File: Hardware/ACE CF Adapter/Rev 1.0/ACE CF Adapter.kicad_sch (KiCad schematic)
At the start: 8 parts, among them J21 STORAGE, J3 Compact Flash

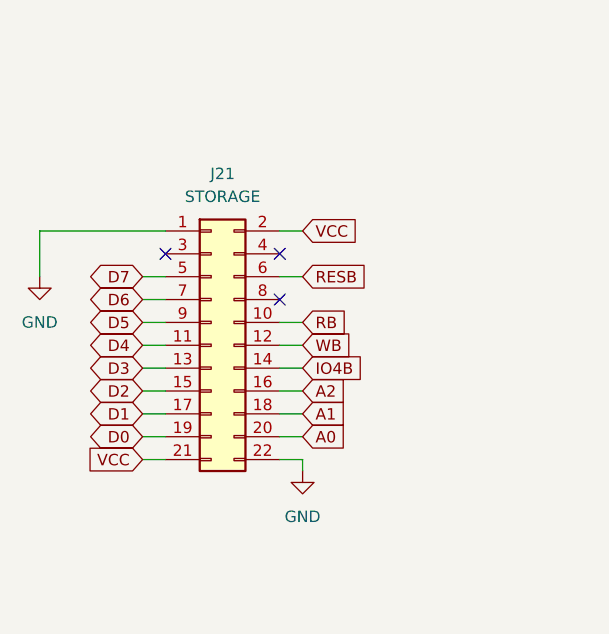
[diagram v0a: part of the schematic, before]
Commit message: Change storage header
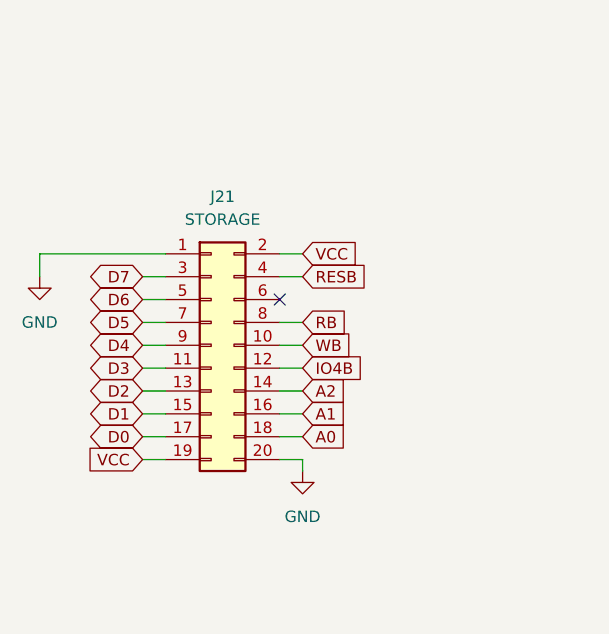
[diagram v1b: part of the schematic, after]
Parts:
- J21: footprint Connector_PinSocket_2.54mm:PinSocket_2x11_P2.54mm_Horizontal -> Connector_PinHeader_2.54mm:PinHeader_2x10_P2.54mm_Horizontal; symbol Connector_Generic:Conn_02x11_Odd_Even -> Connector_Generic:Conn_02x10_Odd_Even; Digikey S5557-ND S5560-ND S5564-ND -> (none); MPN PPPC042LJBN-RC PPPC072LJBN-RC PPPC112LJBN-RC -> (none)
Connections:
- net A0: now also J21.18 (Pin_18); no longer J21.20 (Pin_20)
- net A1: now also J21.16 (Pin_16); no longer J21.18 (Pin_18)
- net A2: now also J21.14 (Pin_14); no longer J21.16 (Pin_16)
- net D0: now also J21.17 (Pin_17); no longer J21.19 (Pin_19)
- net D1: now also J21.15 (Pin_15); no longer J21.17 (Pin_17)
- net D2: now also J21.13 (Pin_13); no longer J21.15 (Pin_15)
- net D3: now also J21.11 (Pin_11); no longer J21.13 (Pin_13)
- net D4: now also J21.9 (Pin_9); no longer J21.11 (Pin_11)
- net D5: now also J21.7 (Pin_7); no longer J21.9 (Pin_9)
- net D6: now also J21.5 (Pin_5); no longer J21.7 (Pin_7)
- net D7: now also J21.3 (Pin_3); no longer J21.5 (Pin_5)
- net GND: now also J21.20 (Pin_20); no longer J21.22 (Pin_22)
- net IO4B: now also J21.12 (Pin_12); no longer J21.14 (Pin_14)
- net RB: now also J21.8 (Pin_8); no longer J21.10 (Pin_10)
- net RESB: now also J21.4 (Pin_4); no longer J21.6 (Pin_6)
- net VCC: now also J21.19 (Pin_19); no longer J21.21 (Pin_21)
- net WB: now also J21.10 (Pin_10); no longer J21.12 (Pin_12)
- no-connect marks 18 -> 16
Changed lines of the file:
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@@
-	)
-	(no_connect
-		(at 58.42 78.74)
 	)
 	(no_connect
@@
 	)
 	(no_connect
-		(at 71.12 78.74)
-	)
-	(no_connect
 		(at 209.55 104.14)
 	)
@@
 	(wire
 		(pts
-			(xy 44.45 76.2) (xy 58.42 76.2)
-		)
-		(stroke
-			(width 0)
-			(type default)
-		)
-	)
-	(wire
-		(pts
-			(xy 44.45 76.2) (xy 44.45 81.28)
+			(xy 44.45 78.74) (xy 58.42 78.74)
+		)
+		(stroke
+			(width 0)
+			(type default)
+		)
+	)
+	(wire
+		(pts
+			(xy 44.45 78.74) (xy 44.45 81.28)
 		)
 		(stroke
@@
 	(wire
 		(pts
-			(xy 71.12 76.2) (xy 73.66 76.2)
+			(xy 71.12 78.74) (xy 73.66 78.74)
 		)
 		(stroke
@@
 	(global_label "VCC"
 		(shape input)
-		(at 73.66 76.2 0)
+		(at 73.66 78.74 0)
 		(effects
 			(font
@@
 		)
 		(property "Intersheetrefs" "${INTERSHEET_REFS}"
-			(at 73.66 76.2 0)
+			(at 73.66 78.74 0)
 			(hide yes)
 			(show_name no)
@@
 	)
 	(symbol
-		(lib_id "Connector_Generic:Conn_02x11_Odd_Even")
+		(lib_id "Connector_Generic:Conn_02x10_Odd_Even")
 		(at 63.5 88.9 0)
 		(unit 1)
@@
 		(fields_autoplaced yes)
 		(property "Reference" "J21"
-			(at 64.77 69.85 0)
+			(at 64.77 72.39 0)
 			(show_name no)
 			(do_not_autoplace no)
@@
 		)
 		(property "Value" "STORAGE"
-			(at 64.77 72.39 0)
-			(show_name no)
-			(do_not_autoplace no)
-			(effects
-				(font
-					(size 1.27 1.27)
-				)
-			)
-		)
-		(property "Footprint" "Connector_PinSocket_2.54mm:PinSocket_2x11_P2.54mm_Horizontal"
+			(at 64.77 74.93 0)
+			(show_name no)
+			(do_not_autoplace no)
+			(effects
+				(font
+					(size 1.27 1.27)
+				)
+			)
+		)
+		(property "Footprint" "Connector_PinHeader_2.54mm:PinHeader_2x10_P2.54mm_Horizontal"
 			(at 63.5 88.9 0)
 			(hide yes)
@@
 			)
 		)
-		(property "Description" "Generic connector, double row, 02x11, odd/even pin numbering scheme (row 1 odd numbers, row 2 even numbers), script generated (kicad-library-utils/schlib/autogen/connector/)"
+		(property "Description" "Generic connector, double row, 02x10, odd/even pin numbering scheme (row 1 odd numbers, row 2 even numbers), script generated (kicad-library-utils/schlib/autogen/connector/)"
 			(at 63.5 88.9 0)
 			(hide yes)
@@
 			)
 		)
-		(property "Digikey" "S5557-ND S5560-ND S5564-ND"
+		(property "Digikey" ""
 			(at 63.5 88.9 0)
 			(hide yes)
@@
 			)
 		)
-		(property "MPN" "PPPC042LJBN-RC PPPC072LJBN-RC PPPC112LJBN-RC"
-			(at 63.5 88.9 0)
-			(hide yes)
-			(show_name no)
-			(do_not_autoplace no)
-			(effects
-				(font
-					(size 1.27 1.27)
-				)
-			)
-		)
 		(pin "17"
 		)
@@
 		(pin "16"
 		)
-		(pin "21"
-		)
-		(pin "22"
-		)
 		(instances

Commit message: Add BOMs
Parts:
- renumbered J21 to J1, J3 to J2
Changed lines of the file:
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@@
 			)
 		)
-		(property "Description" "Resistor"
+		(property "Description" "1/8 W Resistor"
 			(at 151.13 92.71 0)
 			(hide yes)
@@
 		(dnp no)
 		(fields_autoplaced yes)
-		(property "Reference" "J21"
+		(property "Reference" "J1"
 			(at 64.77 72.39 0)
 			(show_name no)
@@
 			)
 		)
-		(property "Description" "Generic connector, double row, 02x10, odd/even pin numbering scheme (row 1 odd numbers, row 2 even numbers), script generated (kicad-library-utils/schlib/autogen/connector/)"
+		(property "Description" "Pin Header 2x10 2.54mm Horizontal"
 			(at 63.5 88.9 0)
 			(hide yes)
@@
 			(project "ACE CF Adapter"
 				(path "/154a5133-b84f-49cb-b657-9c810539146c"
-					(reference "J21")
+					(reference "J1")
 					(unit 1)
 				)
@@
 			)
 		)
-		(property "Description" "Resistor"
+		(property "Description" "1/8 W Resistor"
 			(at 151.13 85.09 0)
 			(hide yes)
@@
 		(dnp no)
 		(fields_autoplaced yes)
-		(property "Reference" "#FLG01"
+		(property "Reference" "#FLG02"
 			(at 187.325 40.64 0)
 			(hide yes)
@@
 			(project "ACE CF Adapter"
 				(path "/154a5133-b84f-49cb-b657-9c810539146c"
-					(reference "#FLG01")
+					(reference "#FLG02")
 					(unit 1)
 				)
@@
 		(dnp no)
 		(fields_autoplaced yes)
-		(property "Reference" "J3"
+		(property "Reference" "J2"
 			(at 193.9641 43.18 0)
 			(show_name no)
@@
 			(project "ACE CF Adapter"
 				(path "/154a5133-b84f-49cb-b657-9c810539146c"
-					(reference "J3")
+					(reference "J2")
 					(unit 1)
 				)
@@
 			)
 		)
-		(property "Description" "Light emitting diode"
+		(property "Description" "3.0mm LED"
 			(at 231.14 93.98 0)
 			(hide yes)
@@
 			)
 		)
-		(property "Description" "Resistor"
+		(property "Description" "1/8 W Resistor"
 			(at 215.9 113.03 0)
 			(hide yes)
@@
 		(dnp no)
 		(fields_autoplaced yes)
-		(property "Reference" "#PWR037"
+		(property "Reference" "#PWR02"
 			(at 73.66 109.22 0)
 			(hide yes)
@@
 			(project "ACE CF Adapter"
 				(path "/154a5133-b84f-49cb-b657-9c810539146c"
-					(reference "#PWR037")
+					(reference "#PWR02")
 					(unit 1)
 				)
@@
 		(dnp no)
 		(fields_autoplaced yes)
-		(property "Reference" "#PWR04"
+		(property "Reference" "#PWR03"
 			(at 158.75 144.78 0)
 			(hide yes)
@@
 			(project "ACE CF Adapter"
 				(path "/154a5133-b84f-49cb-b657-9c810539146c"
-					(reference "#PWR04")
+					(reference "#PWR03")
 					(unit 1)
 				)
@@
 		(dnp no)
 		(fields_autoplaced yes)
-		(property "Reference" "#PWR033"
+		(property "Reference" "#PWR01"
 			(at 44.45 87.63 0)
 			(hide yes)
@@
 			(project "ACE CF Adapter"
 				(path "/154a5133-b84f-49cb-b657-9c810539146c"
-					(reference "#PWR033")
+					(reference "#PWR01")
 					(unit 1)
 				)
@@
 		(dnp no)
 		(fields_autoplaced yes)
-		(property "Reference" "#PWR05"
+		(property "Reference" "#PWR04"
 			(at 189.23 146.05 0)
 			(hide yes)
@@
 			(project "ACE CF Adapter"
 				(path "/154a5133-b84f-49cb-b657-9c810539146c"
-					(reference "#PWR05")
+					(reference "#PWR04")
 					(unit 1)
 				)
@@
 		(dnp no)
 		(fields_autoplaced yes)
-		(property "Reference" "#FLG02"
+		(property "Reference" "#FLG01"
 			(at 182.245 137.16 0)
 			(hide yes)
@@
 			(project "ACE CF Adapter"
 				(path "/154a5133-b84f-49cb-b657-9c810539146c"
-					(reference "#FLG02")
+					(reference "#FLG01")
 					(unit 1)
 				)
@@
 			)
 		)
-		(property "Description" "Resistor"
+		(property "Description" "1/8 W Resistor"
 			(at 215.9 87.63 0)
 			(hide yes)
@@
 			)
 		)
-		(property "Description" "Resistor"
+		(property "Description" "1/8 W Resistor"
 			(at 231.14 105.41 0)
 			(hide yes)

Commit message: Finish BOM and add to README
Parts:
- D1: Digikey (none) -> 732-5008-ND; Other (none) -> https://www.amazon.com/300-Pcs-LED-Diode-Assortment/dp/B0F3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
- J1: Other (none) -> https://www.amazon.com/dp/B00W8TSWXS
- R1, R2, R3, R4: Digikey (none) -> RNF18FTD1K00CT-ND; Other (none) -> https://www.amazon.com/ALLECIN-8W-Metal-Film-Resistor/dp/B0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
- R5: Other (none) -> https://www.amazon.com/ALLECIN-8W-Metal-Film-Resistor/dp/B0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
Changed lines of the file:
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@@
+			)
+		)
+		(property "Digikey" "RNF18FTD1K00CT-ND"
+			(at 151.13 92.71 90)
+			(hide yes)
+			(show_name no)
+			(do_not_autoplace no)
+			(effects
+				(font
+					(size 1.27 1.27)
+				)
+			)
+		)
+		(property "Other" "https://www.amazon.com/ALLECIN-8W-Metal-Film-Resistor/dp/B0C77TM3NR"
+			(at 151.13 92.71 90)
+			(hide yes)
+			(show_name no)
+			(do_not_autoplace no)
+			(effects
+				(font
+					(size 1.27 1.27)
+				)
+			)
+		)
+		(property "Mouser" ""
+			(at 151.13 92.71 90)
+			(hide yes)
+			(show_name no)
+			(do_not_autoplace no)
+			(effects
+				(font
+					(size 1.27 1.27)
+				)
 			)
 		)
@@
 			)
 		)
+		(property "Other" "https://www.amazon.com/dp/B00W8TSWXS"
+			(at 63.5 88.9 0)
+			(hide yes)
+			(show_name no)
+			(do_not_autoplace no)
+			(effects
+				(font
+					(size 1.27 1.27)
+				)
+			)
+		)
+		(property "Mouser" ""
+			(at 63.5 88.9 0)
+			(hide yes)
+			(show_name no)
+			(do_not_autoplace no)
+			(effects
+				(font
+					(size 1.27 1.27)
+				)
+			)
+		)
 		(pin "17"
 		)
@@
 		(property "Description" "1/8 W Resistor"
 			(at 151.13 85.09 0)
+			(hide yes)
+			(show_name no)
+			(do_not_autoplace no)
+			(effects
+				(font
+					(size 1.27 1.27)
+				)
+			)
+		)
+		(property "Digikey" "RNF18FTD1K00CT-ND"
+			(at 151.13 85.09 90)
+			(hide yes)
+			(show_name no)
+			(do_not_autoplace no)
+			(effects
+				(font
+					(size 1.27 1.27)
+				)
+			)
+		)
+		(property "Other" "https://www.amazon.com/ALLECIN-8W-Metal-Film-Resistor/dp/B0C77TM3NR"
+			(at 151.13 85.09 90)
+			(hide yes)
+			(show_name no)
+			(do_not_autoplace no)
+			(effects
+				(font
+					(size 1.27 1.27)
+				)
+			)
+		)
+		(property "Mouser" ""
+			(at 151.13 85.09 90)
 			(hide yes)
 			(show_name no)
@@
 			)
 		)
+		(property "Other" ""
+			(at 190.5 87.63 0)
+			(hide yes)
+			(show_name no)
+			(do_not_autoplace no)
+			(effects
+				(font
+					(size 1.27 1.27)
+				)
+			)
+		)
+		(property "Mouser" ""
+			(at 190.5 87.63 0)
+			(hide yes)
+			(show_name no)
+			(do_not_autoplace no)
+			(effects
+				(font
+					(size 1.27 1.27)
+				)
+			)
+		)
 		(pin "12"
 		)
@@
 			)
 		)
+		(property "Digikey" "732-5008-ND"
+			(at 231.14 93.98 90)
+			(hide yes)
+			(show_name no)
+			(do_not_autoplace no)
+			(effects
+				(font
+					(size 1.27 1.27)
+				)
+			)
+		)
+		(property "Other" "https://www.amazon.com/300-Pcs-LED-Diode-Assortment/dp/B0F38LJDJB"
+			(at 231.14 93.98 90)
+			(hide yes)
+			(show_name no)
+			(do_not_autoplace no)
+			(effects
+				(font
+					(size 1.27 1.27)
+				)
+			)
+		)
+		(property "Mouser" ""
+			(at 231.14 93.98 90)
+			(hide yes)
+			(show_name no)
+			(do_not_autoplace no)
+			(effects
+				(font
+					(size 1.27 1.27)
+				)
+			)
+		)
 		(pin "1"
 		)
@@
 		(property "Description" "1/8 W Resistor"
 			(at 215.9 113.03 0)
+			(hide yes)
+			(show_name no)
+			(do_not_autoplace no)
+			(effects
+				(font
+					(size 1.27 1.27)
+				)
+			)
+		)
+		(property "Digikey" "RNF18FTD1K00CT-ND"
+			(at 215.9 113.03 90)
+			(hide yes)
+			(show_name no)
+			(do_not_autoplace no)
+			(effects
+				(font
+					(size 1.27 1.27)
+				)
+			)
+		)
+		(property "Other" "https://www.amazon.com/ALLECIN-8W-Metal-Film-Resistor/dp/B0C77TM3NR"
+			(at 215.9 113.03 90)
+			(hide yes)
+			(show_name no)
+			(do_not_autoplace no)
+			(effects
+				(font
+					(size 1.27 1.27)
+				)
+			)
+		)
+		(property "Mouser" ""
+			(at 215.9 113.03 90)
 			(hide yes)
 			(show_name no)
@@
 			)
 		)
+		(property "Digikey" "RNF18FTD1K00CT-ND"
+			(at 215.9 87.63 90)
+			(hide yes)
+			(show_name no)
+			(do_not_autoplace no)
+			(effects
+				(font
+					(size 1.27 1.27)
+				)
+			)
+		)
+		(property "Other" "https://www.amazon.com/ALLECIN-8W-Metal-Film-Resistor/dp/B0C77TM3NR"
+			(at 215.9 87.63 90)
+			(hide yes)
+			(show_name no)
+			(do_not_autoplace no)
+			(effects
+				(font
+					(size 1.27 1.27)
+				)
+			)
+		)
+		(property "Mouser" ""
+			(at 215.9 87.63 90)
+			(hide yes)
+			(show_name no)
+			(do_not_autoplace no)
+			(effects
+				(font
+					(size 1.27 1.27)
+				)
+			)
+		)
 		(pin "2"
 		)
@@
 			(at 231.14 105.41 0)
 			(hide yes)
+			(show_name no)
+			(do_not_autoplace no)
+			(effects
+				(font
+					(size 1.27 1.27)
+				)
+			)
+		)
+		(property "Other" "https://www.amazon.com/ALLECIN-8W-Metal-Film-Resistor/dp/B0C77TM3NR"
+			(at 231.14 105.41 0)
+			(hide yes)
+			(show_name no)
+			(do_not_autoplace no)
+			(effects
+				(font
+					(size 1.27 1.27)
+				)
+			)
+		)
+		(property "Mouser" ""
+			(at 231.14 105.41 0)
+			(hide yes)
